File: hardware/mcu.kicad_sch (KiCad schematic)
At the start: 26 parts, among them J201 Conn_ARM_JTAG_SWD_10, SW201 SW_Push, U201 EFR32FG28A122F1024GM48-A, U202 USBLC6-2P6, U203 USBLC6-2P6, Y201 LF_Crystal, Y202 ECS-390-CDX-1932

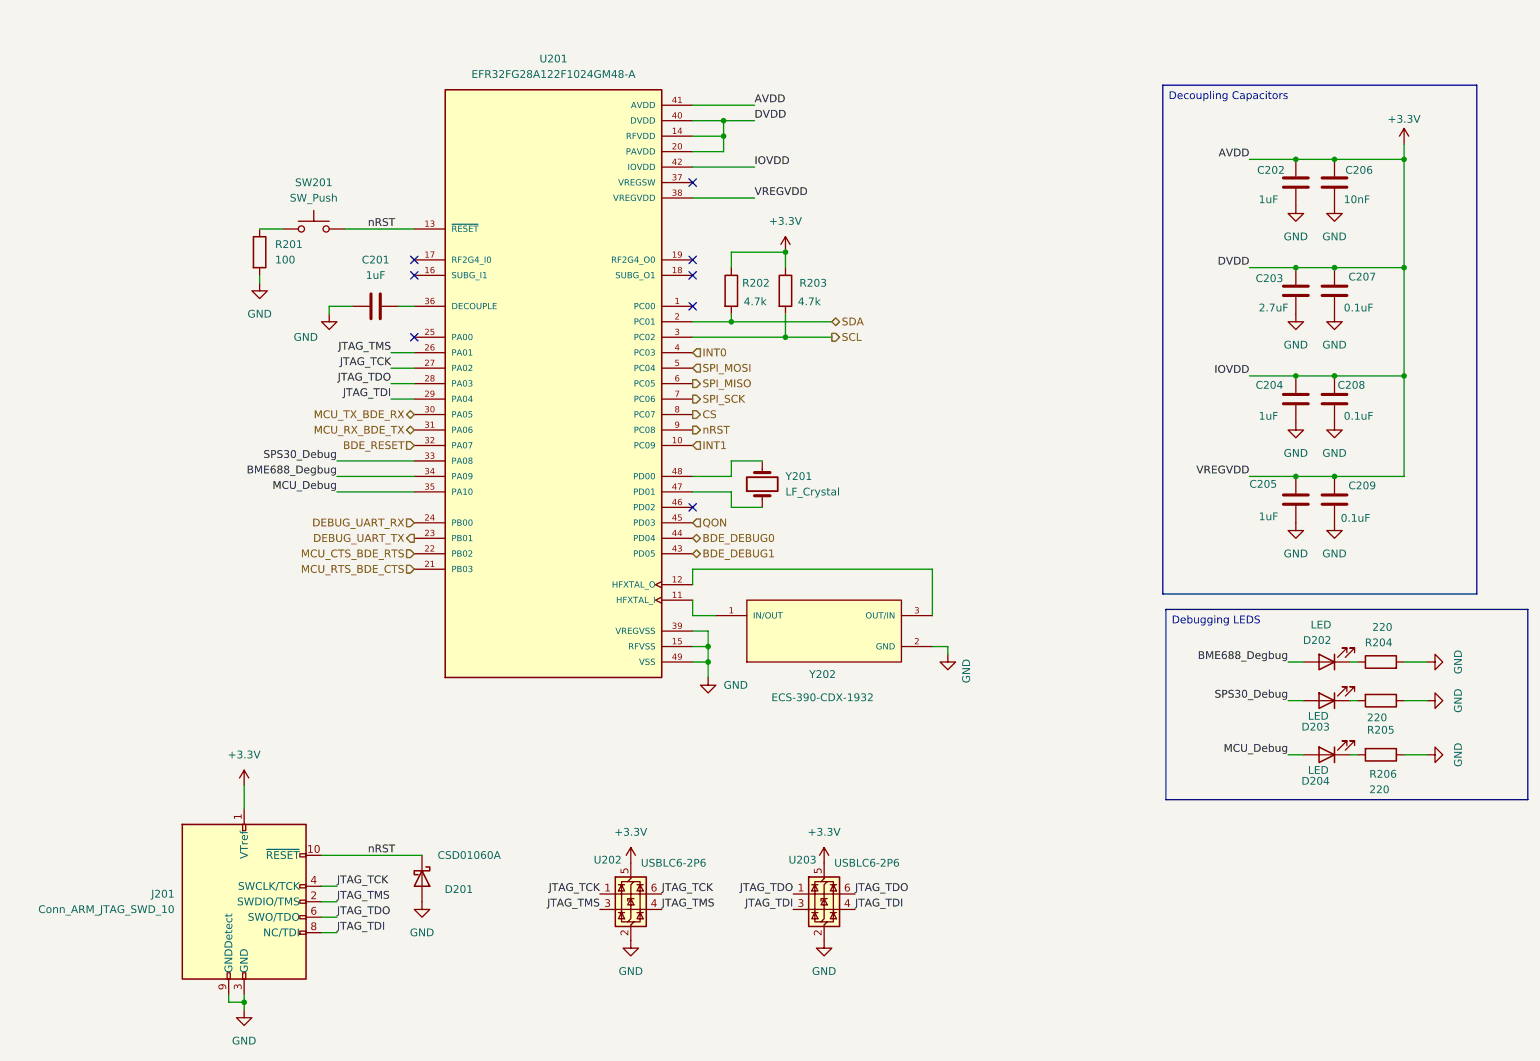
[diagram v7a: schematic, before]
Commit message: updated labels
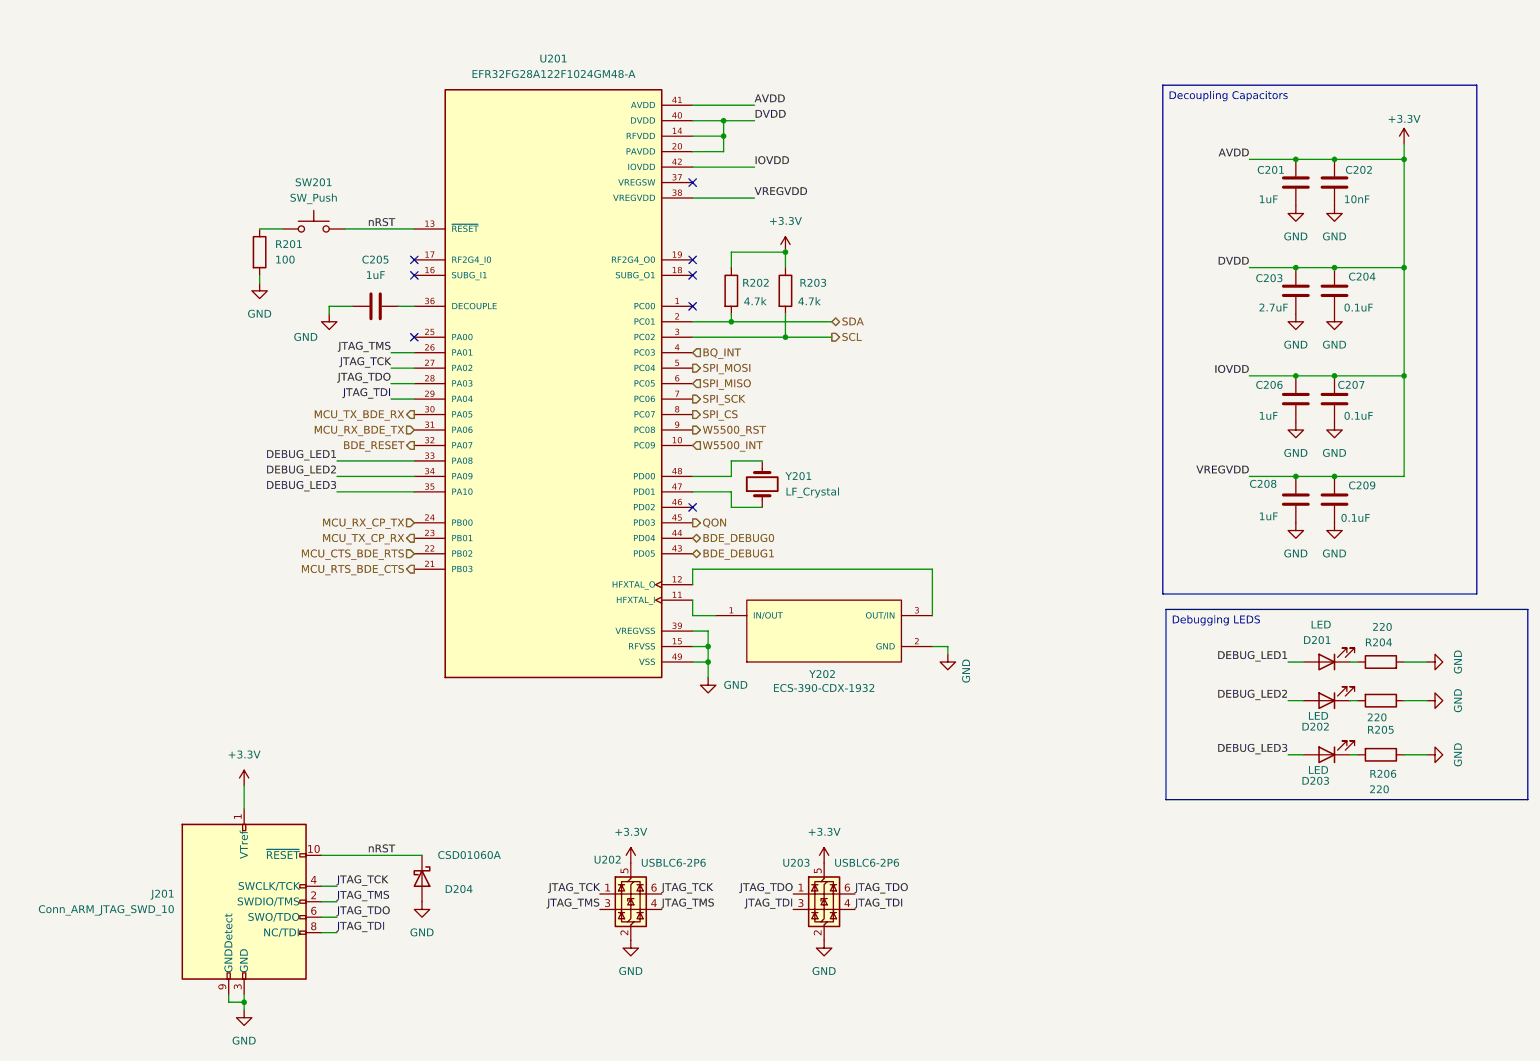
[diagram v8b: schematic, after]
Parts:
- renumbered C202 to C201, C206 to C202, C207 to C204, C201 to C205, C204 to C206, C208 to C207, C205 to C208, D202 to D201, D203 to D202, D204 to D203, D201 to D204
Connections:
- net nRST: no longer U201.9 (PC08)
- net BME688_Degbug renamed DEBUG_LED1
- net DEBUG_LED1: now also U201.33 (PA08); no longer U201.34 (PA09)
- net CS renamed SPI_CS
- net DEBUG_UART_RX renamed MCU_RX_CP_TX
- net DEBUG_UART_TX renamed MCU_TX_CP_RX
- net INT0 renamed BQ_INT
- net INT1 renamed W5500_INT
- net MCU_Debug renamed DEBUG_LED3
- net SPS30_Debug renamed DEBUG_LED2
- net DEBUG_LED2: now also U201.34 (PA09); no longer U201.33 (PA08)
- new net W5500_RST: U201.9 (PC08)
